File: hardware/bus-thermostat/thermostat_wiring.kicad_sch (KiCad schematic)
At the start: 44 parts, among them Q1 2N7002, Q2 2N7002, Q3 2N7002, Q4 IRF540N, Q5 IRF540N, U1 UCC27714D, U2 PCA9557D

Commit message: More slight tweaks for resimulation
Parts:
- gave numbers to parts that had none: 1
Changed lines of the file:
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@@
   (symbol (lib_id "Transformer:PA2004NL") (at 184.023 51.435 0) (unit 1)
     (in_bom yes) (on_board yes) (fields_autoplaced)
-    (property "Reference" "T?" (id 0) (at 184.023 33.02 0))
+    (property "Reference" "T1" (id 0) (at 184.023 33.02 0))
     (property "Value" "PA2004NL" (id 1) (at 184.023 35.56 0))
     (property "Footprint" "Transformer_SMD:Pulse_PA2004NL" (id 2) (at 184.023 51.435 0)

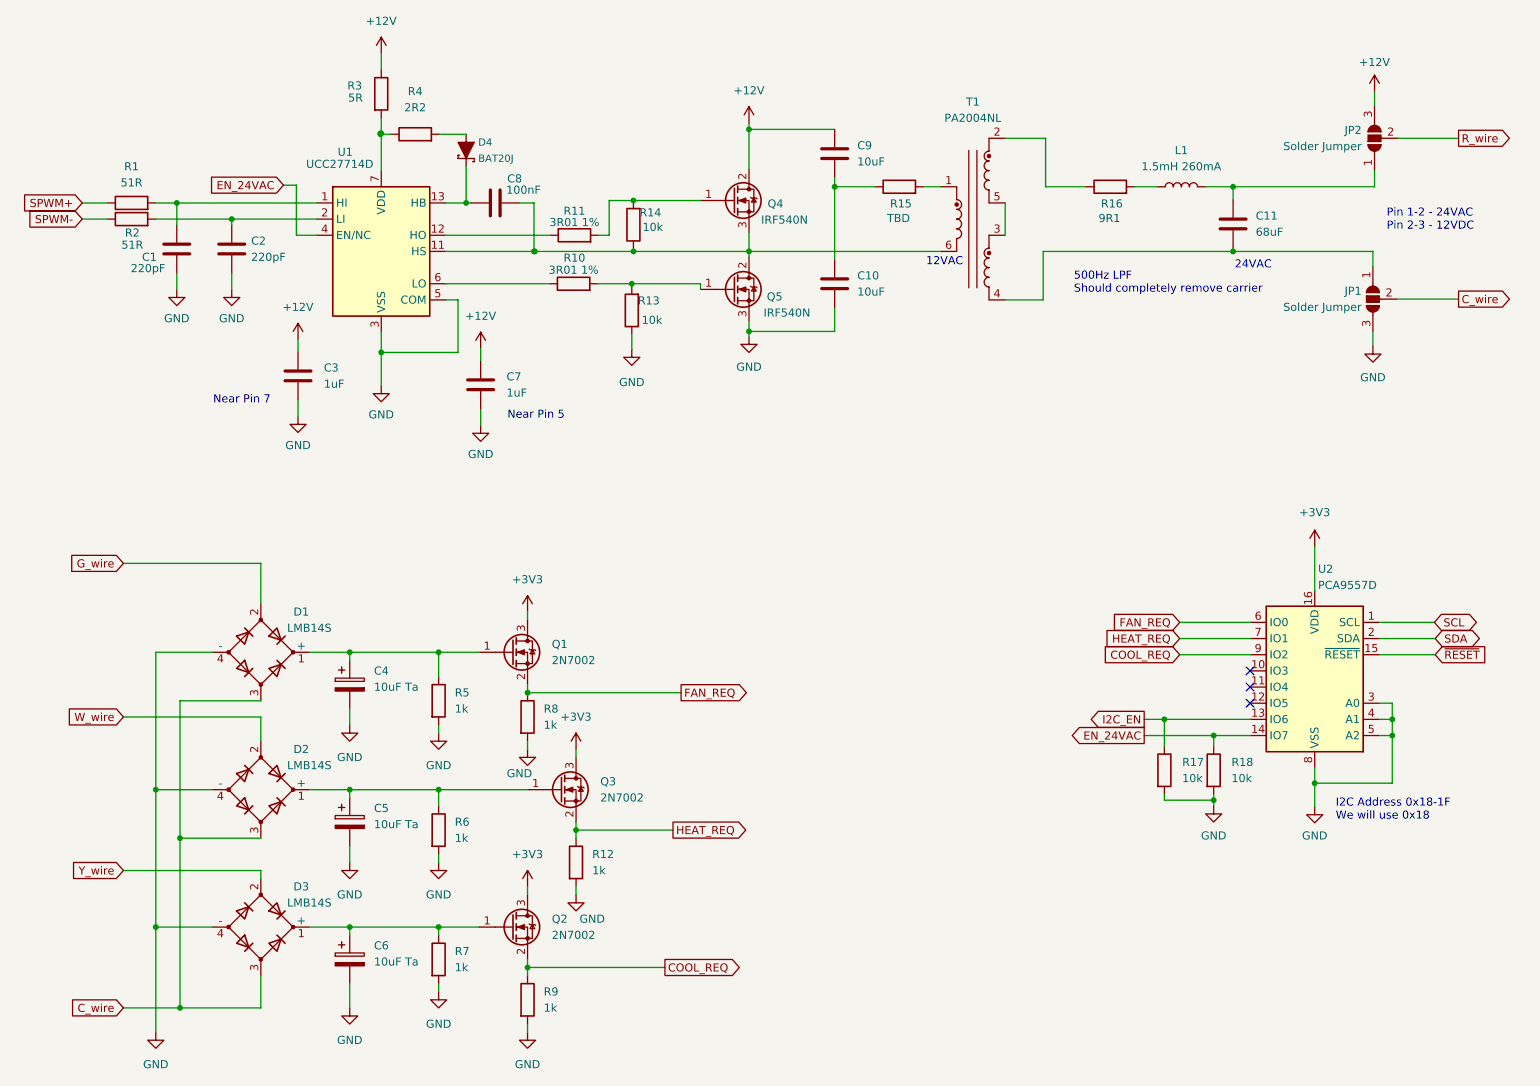
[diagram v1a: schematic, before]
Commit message: Fix oscillator, add fan controller/thermostat and its IOs.
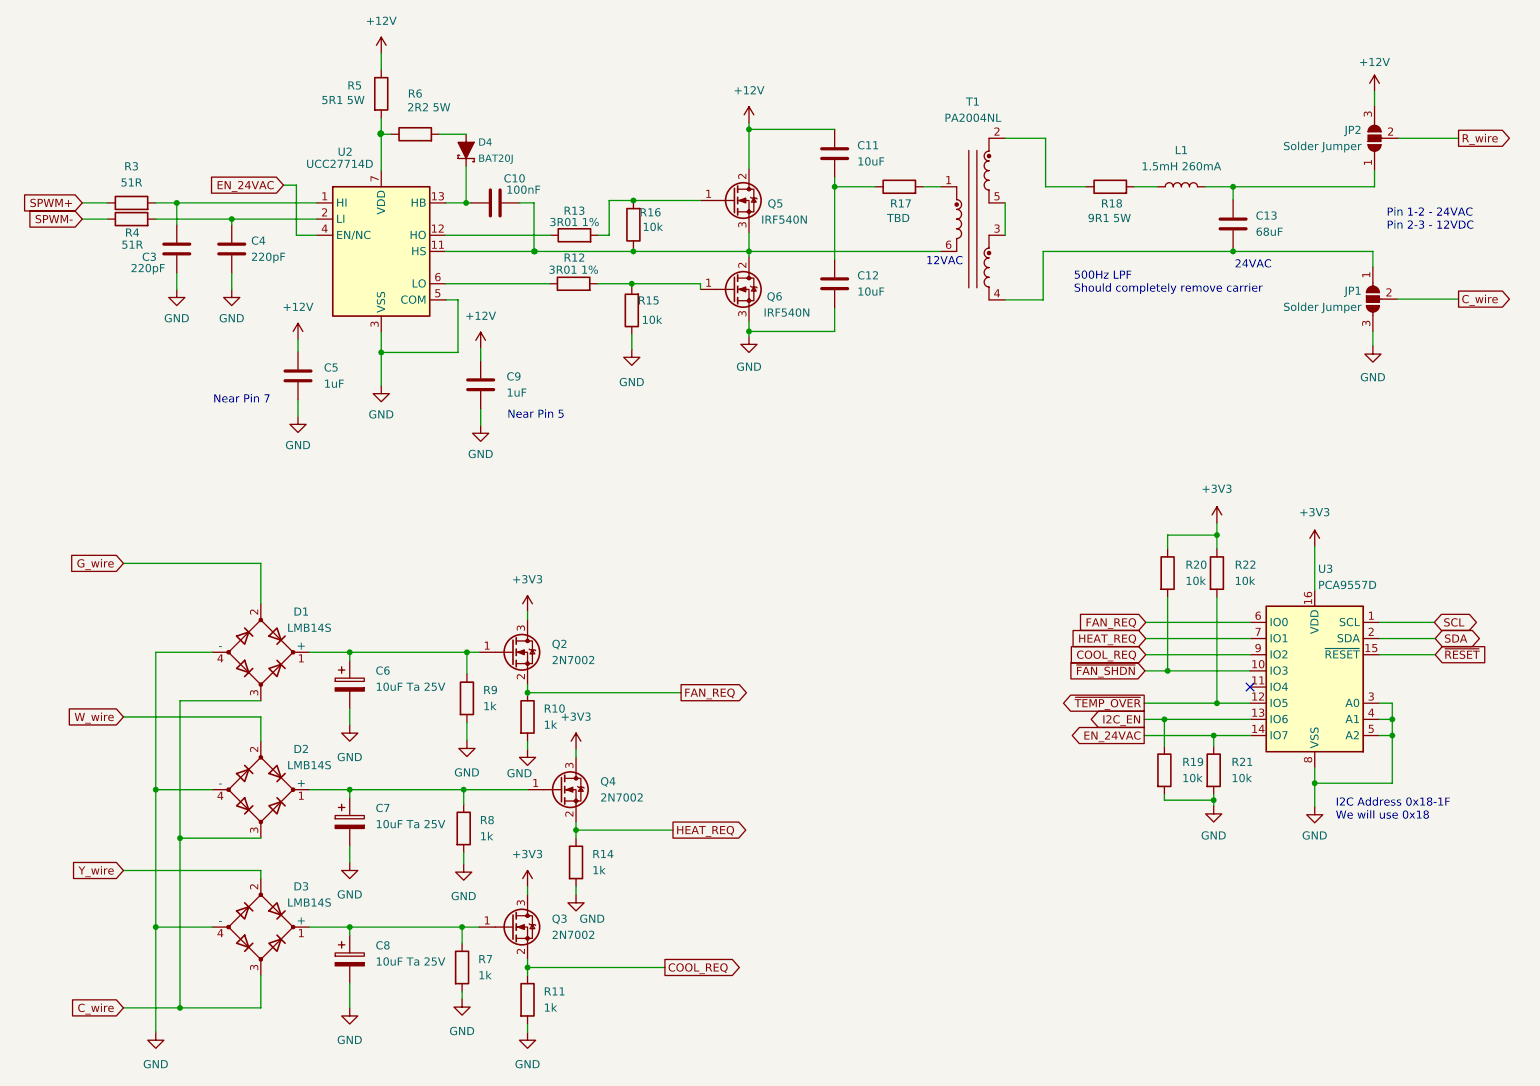
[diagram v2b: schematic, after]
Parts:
- added R20, R22: 10k, Resistor_SMD:R_0805_2012Metric_Pad1.20x1.40mm_HandSolder, symbol Device:R
- C10: renamed from C8; footprint (none) -> Capacitor_SMD:C_0805_2012Metric_Pad1.18x1.45mm_HandSolder
- C11: renamed from C9; footprint (none) -> Capacitor_SMD:C_0805_2012Metric_Pad1.18x1.45mm_HandSolder
- C12: renamed from C10; footprint (none) -> Capacitor_SMD:C_0805_2012Metric_Pad1.18x1.45mm_HandSolder
- C13: renamed from C11; footprint (none) -> Capacitor_SMD:C_0805_2012Metric_Pad1.18x1.45mm_HandSolder
- C3: renamed from C1; footprint (none) -> Capacitor_SMD:C_0805_2012Metric_Pad1.18x1.45mm_HandSolder
- C4: renamed from C2; footprint (none) -> Capacitor_SMD:C_0805_2012Metric_Pad1.18x1.45mm_HandSolder
- C5: renamed from C3; footprint (none) -> Capacitor_SMD:C_0805_2012Metric_Pad1.18x1.45mm_HandSolder
- C6: renamed from C4; value 10uF Ta -> 10uF Ta 25V; footprint (none) -> Capacitor_Tantalum_SMD:CP_EIA-6032-20_AVX-F_Pad2.25x2.35mm_HandSolder
- C7: renamed from C5; value 10uF Ta -> 10uF Ta 25V; footprint (none) -> Capacitor_Tantalum_SMD:CP_EIA-6032-20_AVX-F_Pad2.25x2.35mm_HandSolder
- C8: renamed from C6; value 10uF Ta -> 10uF Ta 25V; footprint (none) -> Capacitor_Tantalum_SMD:CP_EIA-6032-20_AVX-F_Pad2.25x2.35mm_HandSolder
- C9: renamed from C7; footprint (none) -> Capacitor_SMD:C_0805_2012Metric_Pad1.18x1.45mm_HandSolder
- R10: renamed from R8; footprint (none) -> Resistor_SMD:R_0805_2012Metric_Pad1.20x1.40mm_HandSolder
- R11: renamed from R9; footprint (none) -> Resistor_SMD:R_0805_2012Metric_Pad1.20x1.40mm_HandSolder
- R12: renamed from R10; footprint (none) -> Resistor_SMD:R_0805_2012Metric_Pad1.20x1.40mm_HandSolder
- R13: renamed from R11; footprint (none) -> Resistor_SMD:R_0805_2012Metric_Pad1.20x1.40mm_HandSolder
- R14: renamed from R12; footprint (none) -> Resistor_SMD:R_0805_2012Metric_Pad1.20x1.40mm_HandSolder
- R15: renamed from R13; footprint (none) -> Resistor_SMD:R_0805_2012Metric_Pad1.20x1.40mm_HandSolder
- R16: renamed from R14; footprint (none) -> Resistor_SMD:R_0805_2012Metric_Pad1.20x1.40mm_HandSolder
- R17: renamed from R15; footprint (none) -> Resistor_SMD:R_0805_2012Metric_Pad1.20x1.40mm_HandSolder
- R18: renamed from R16; value 9R1 -> 9R1 5W; footprint (none) -> UltraLibrarian:355010RFT
- R19: renamed from R17; footprint (none) -> Resistor_SMD:R_0805_2012Metric_Pad1.20x1.40mm_HandSolder
- R21: renamed from R18; footprint (none) -> Resistor_SMD:R_0805_2012Metric_Pad1.20x1.40mm_HandSolder
- R3: renamed from R1; footprint (none) -> Resistor_SMD:R_0805_2012Metric_Pad1.20x1.40mm_HandSolder
- R4: renamed from R2; footprint (none) -> Resistor_SMD:R_0805_2012Metric_Pad1.20x1.40mm_HandSolder
- R5: renamed from R3; value 5R -> 5R1 5W; footprint (none) -> UltraLibrarian:355010RFT
- R6: renamed from R4; value 2R2 -> 2R2 5W; footprint (none) -> UltraLibrarian:355010RFT
- R7: footprint (none) -> Resistor_SMD:R_0805_2012Metric_Pad1.20x1.40mm_HandSolder
- R8: renamed from R6; footprint (none) -> Resistor_SMD:R_0805_2012Metric_Pad1.20x1.40mm_HandSolder
- R9: renamed from R5; footprint (none) -> Resistor_SMD:R_0805_2012Metric_Pad1.20x1.40mm_HandSolder
- renumbered Q1 to Q2, Q2 to Q3, Q3 to Q4, Q4 to Q5, Q5 to Q6, U1 to U2, U2 to U3
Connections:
- net +3V3: now also R20.1, R22.1
- net ~{FAN_SHDN}: now reaches U3.10 (IO3)
- net ~{FAN_SHDN}: now also R20.2
- net ~{TEMP_OVER}: now reaches U3.12 (IO5)
- net ~{TEMP_OVER}: now also R22.2
- no-connect marks 3 -> 1
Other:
- moved on the sheet: R7, R8, R9

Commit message: Ooops forgot to save.
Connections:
- net ~{FAN_SHDN}: now also R22.2, U3.12 (IO5); no longer R20.2, U3.10 (IO3)
- net ~{TEMP_OVER}: now also R20.2, U3.10 (IO3); no longer R22.2, U3.12 (IO5)
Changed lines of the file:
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@@
     )
   )
-  (global_label "~{FAN_SHDN}" (shape input) (at 211.074 122.428 180) (fields_autoplaced)
+  (global_label "~{FAN_SHDN}" (shape output) (at 210.947 127.508 180) (fields_autoplaced)
     (effects (font (size 1.27 1.27)) (justify right))
-    (property "Intersheet References" "${INTERSHEET_REFS}" (id 0) (at 199.0452 122.3486 0)
+    (property "Intersheet References" "${INTERSHEET_REFS}" (id 0) (at 198.9182 127.4286 0)
       (effects (font (size 1.27 1.27)) (justify right) hide)
     )
@@
     )
   )
-  (global_label "~{TEMP_OVER}" (shape output) (at 210.947 127.508 180) (fields_autoplaced)
+  (global_label "~{TEMP_OVER}" (shape input) (at 211.074 122.428 180) (fields_autoplaced)
     (effects (font (size 1.27 1.27)) (justify right))
-    (property "Intersheet References" "${INTERSHEET_REFS}" (id 0) (at 197.8901 127.4286 0)
+    (property "Intersheet References" "${INTERSHEET_REFS}" (id 0) (at 198.0171 122.3486 0)
       (effects (font (size 1.27 1.27)) (justify right) hide)
     )
